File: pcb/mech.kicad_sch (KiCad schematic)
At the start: 50 parts

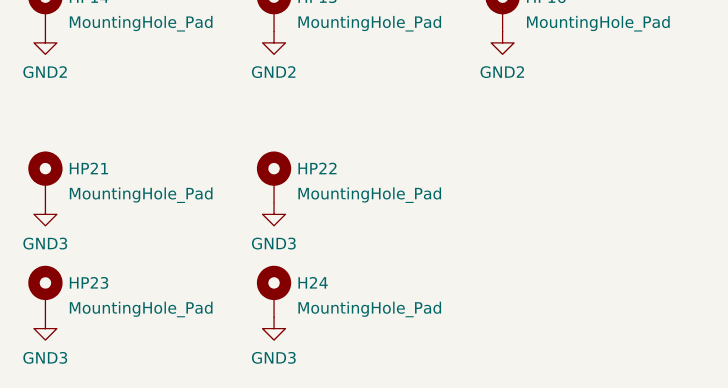
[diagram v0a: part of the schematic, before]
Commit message: add dual promicro footprint, associate footprints
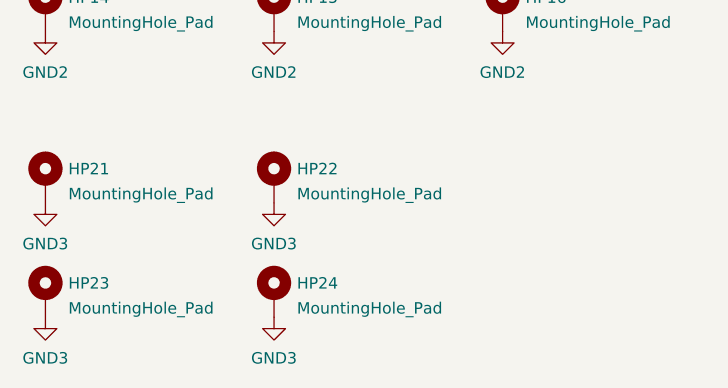
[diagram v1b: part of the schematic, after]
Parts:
- H11, H12, H13, H14, H15, H16, H21, H22, H23, H24, HP11, HP12, HP13, HP14, HP15, HP16, HP21, HP22, HP23: footprint (none) -> MountingHole:MountingHole_2.2mm_M2_DIN965_Pad
- HP24: renamed from H24; footprint (none) -> MountingHole:MountingHole_2.2mm_M2_DIN965_Pad
- HS11, HS12, HS13, HS14, HS15, HS16, HS21, HS22, HS23, HS24, HS25, HS26, HS31, HS32, HS33, HS34, HS35, HS36, HS41, HS42, HS43, HS44, HS45, HS46, HS51, HS52, HS53, HS54, HS55, HS56: footprint (none) -> keebio:MX_Switch_Cutout

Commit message: finish layout and panel
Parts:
- added H14, H18: MountingHole_Pad, MountingHole:MountingHole_2.2mm_M2_DIN965_Pad, symbol Mechanical:MountingHole_Pad
- renumbered H14 to H15, H15 to H16, H16 to H17
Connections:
- net GND: now also H14.1, H18.1
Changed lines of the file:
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@@
   (symbol (lib_id "Mechanical:MountingHole_Pad") (at 88.9 48.26 0) (unit 1)
     (in_bom yes) (on_board yes) (fields_autoplaced)
-    (property "Reference" "H16" (id 0) (at 91.44 47.034 0)
+    (property "Reference" "H17" (id 0) (at 91.44 47.034 0)
       (effects (font (size 1.27 1.27)) (justify left))
     )
@@
     (pin "1")
   )
+  (symbol (lib_id "power:GND") (at 114.3 38.1 0) (unit 1)
+    (in_bom yes) (on_board yes) (fields_autoplaced)
+    (property "Reference" "#PWR?" (id 0) (at 114.3 44.45 0)
+      (effects (font (size 1.27 1.27)) hide)
+    )
+    (property "Value" "GND" (id 1) (at 114.3 42.6624 0))
+    (property "Footprint" "" (id 2) (at 114.3 38.1 0)
+      (effects (font (size 1.27 1.27)) hide)
+    )
+    (property "Datasheet" "" (id 3) (at 114.3 38.1 0)
+      (effects (font (size 1.27 1.27)) hide)
+    )
+    (pin "1")
+  )
   (symbol (lib_id "keebio:Hole") (at 231.14 48.26 0) (unit 1)
     (in_bom yes) (on_board yes) (fields_autoplaced)
@@
     )
   )
+  (symbol (lib_id "Mechanical:MountingHole_Pad") (at 114.3 48.26 0) (unit 1)
+    (in_bom yes) (on_board yes) (fields_autoplaced)
+    (property "Reference" "H18" (id 0) (at 116.84 47.034 0)
+      (effects (font (size 1.27 1.27)) (justify left))
+    )
+    (property "Value" "MountingHole_Pad" (id 1) (at 116.84 49.8091 0)
+      (effects (font (size 1.27 1.27)) (justify left))
+    )
+    (property "Footprint" "MountingHole:MountingHole_2.2mm_M2_DIN965_Pad" (id 2) (at 114.3 48.26 0)
+      (effects (font (size 1.27 1.27)) hide)
+    )
+    (property "Datasheet" "~" (id 3) (at 114.3 48.26 0)
+      (effects (font (size 1.27 1.27)) hide)
+    )
+    (pin "1")
+  )
   (symbol (lib_id "Mechanical:MountingHole_Pad") (at 63.5 156.21 0) (unit 1)
     (in_bom yes) (on_board yes) (fields_autoplaced)
@@
   (symbol (lib_id "Mechanical:MountingHole_Pad") (at 38.1 48.26 0) (unit 1)
     (in_bom yes) (on_board yes) (fields_autoplaced)
-    (property "Reference" "H14" (id 0) (at 40.64 47.034 0)
+    (property "Reference" "H15" (id 0) (at 40.64 47.034 0)
       (effects (font (size 1.27 1.27)) (justify left))
     )
@@
     (pin "1")
   )
+  (symbol (lib_id "Mechanical:MountingHole_Pad") (at 114.3 35.56 0) (unit 1)
+    (in_bom yes) (on_board yes) (fields_autoplaced)
+    (property "Reference" "H14" (id 0) (at 116.84 34.334 0)
+      (effects (font (size 1.27 1.27)) (justify left))
+    )
+    (property "Value" "MountingHole_Pad" (id 1) (at 116.84 37.1091 0)
+      (effects (font (size 1.27 1.27)) (justify left))
+    )
+    (property "Footprint" "MountingHole:MountingHole_2.2mm_M2_DIN965_Pad" (id 2) (at 114.3 35.56 0)
+      (effects (font (size 1.27 1.27)) hide)
+    )
+    (property "Datasheet" "~" (id 3) (at 114.3 35.56 0)
+      (effects (font (size 1.27 1.27)) hide)
+    )
+    (pin "1")
+  )
   (symbol (lib_id "keebio:Hole") (at 214.63 38.1 0) (unit 1)
     (in_bom yes) (on_board yes) (fields_autoplaced)
@@
   (symbol (lib_id "Mechanical:MountingHole_Pad") (at 63.5 48.26 0) (unit 1)
     (in_bom yes) (on_board yes) (fields_autoplaced)
-    (property "Reference" "H15" (id 0) (at 66.04 47.034 0)
+    (property "Reference" "H16" (id 0) (at 66.04 47.034 0)
       (effects (font (size 1.27 1.27)) (justify left))
     )
@@
       (effects (font (size 1.27 1.27)) hide)
     )
+    (pin "1")
+  )
+  (symbol (lib_id "power:GND") (at 114.3 50.8 0) (unit 1)
+    (in_bom yes) (on_board yes) (fields_autoplaced)
+    (property "Reference" "#PWR?" (id 0) (at 114.3 57.15 0)
+      (effects (font (size 1.27 1.27)) hide)
+    )
+    (property "Value" "GND" (id 1) (at 114.3 55.3624 0))
+    (property "Footprint" "" (id 2) (at 114.3 50.8 0)
+      (effects (font (size 1.27 1.27)) hide)
+    )
+    (property "Datasheet" "" (id 3) (at 114.3 50.8 0)
+      (effects (font (size 1.27 1.27)) hide)
+    )
